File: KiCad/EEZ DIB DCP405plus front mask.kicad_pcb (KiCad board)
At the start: 2 copper layers, 35 x 111.5 mm, 3 parts

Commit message: Gerbers update
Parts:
- added REF**: MountingHole, PCM_EEZ_THT:Mounting_hole 1.8_4.4mm_via_NO_NET, F.Cu at (149.1, 146.8)
- added REF**: MountingHole, PCM_EEZ_THT:Mounting_hole 1.8_4.4mm_via_NO_NET, F.Cu at (166.9, 146.8)
- added REF**: MountingHole, PCM_EEZ_THT:Mounting_hole 1.8_4.4mm_via_NO_NET, F.Cu at (149.1, 41.8)
- added REF**: MountingHole, PCM_EEZ_THT:Mounting_hole 1.8_4.4mm_via_NO_NET, F.Cu at (166.9, 41.8)
- REF** (x2): footprint PCM_EEZ_THT:Mounting_hole 2_4.4mm_via_NO_NET -> PCM_EEZ_THT:Mounting_hole 1.8_4.4mm_via_NO_NET
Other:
- outline, holes or cut-outs redrawn

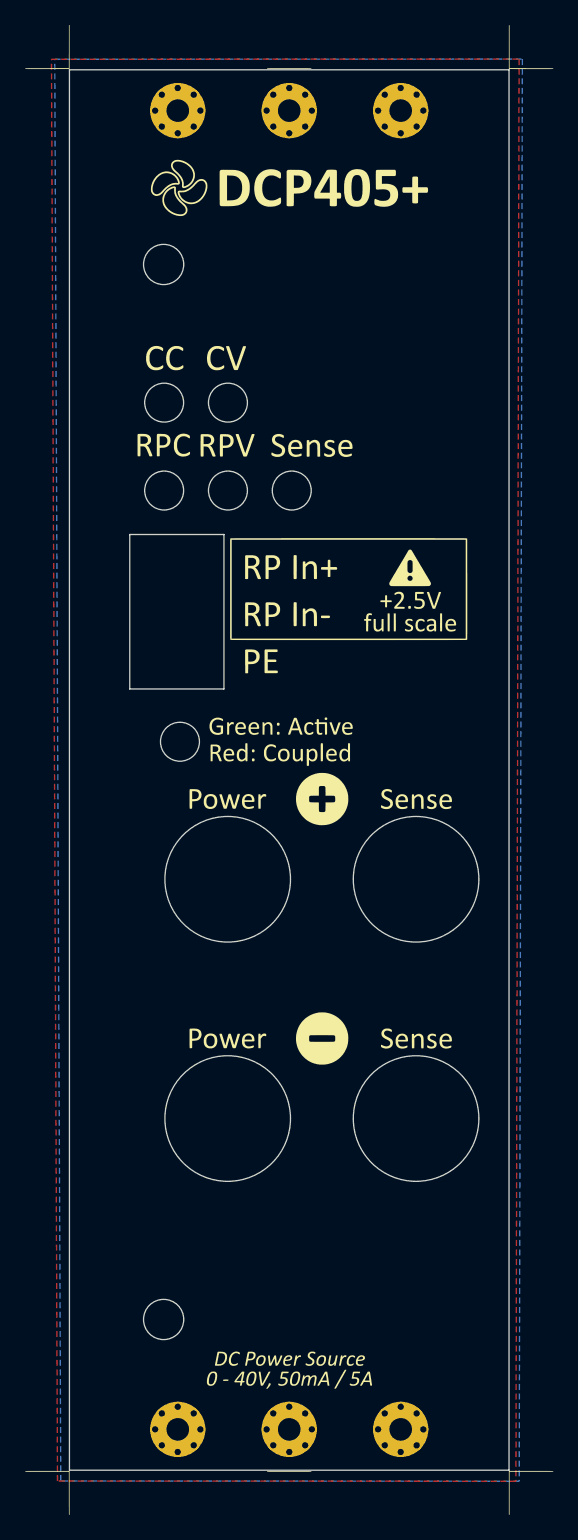
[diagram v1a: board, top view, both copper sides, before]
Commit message: Pullups for OE indicator added
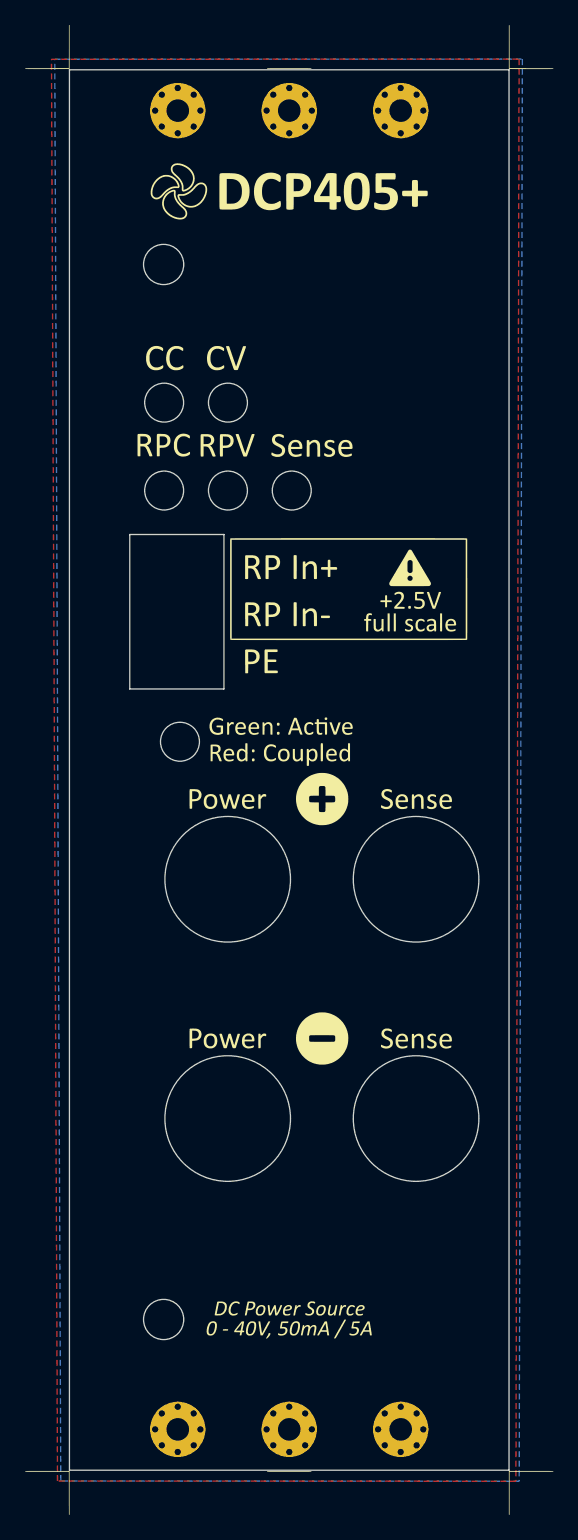
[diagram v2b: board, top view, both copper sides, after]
